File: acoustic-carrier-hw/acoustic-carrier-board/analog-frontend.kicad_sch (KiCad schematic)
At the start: 97 parts, among them J1001 BWU.FL-IPEX1, J1002 BWU.FL-IPEX1, J1003 BWU.FL-IPEX1, J1004 BWU.FL-IPEX1, J1005 BWU.FL-IPEX1, J1006 BWU.FL-IPEX1, J1007 8P8C_Shielded, J1008 BWU.FL-IPEX1, J1009 BWU.FL-IPEX1, J1010 BWU.FL-IPEX1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

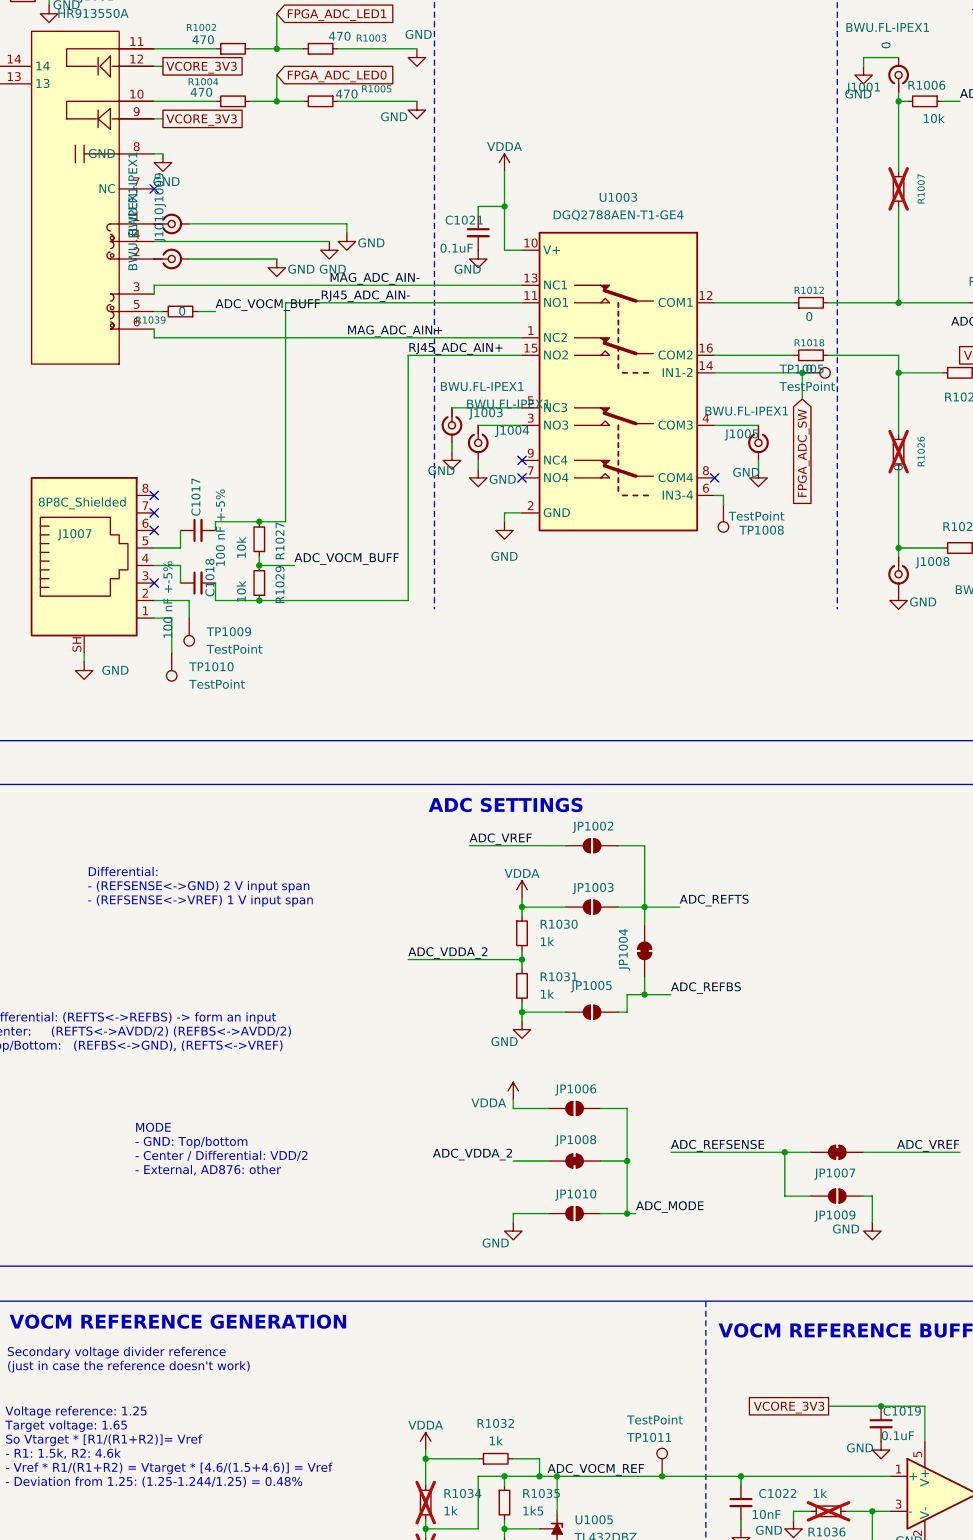
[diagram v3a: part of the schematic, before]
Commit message: [carrier] Layout more or less complete (next) think about adding 6x2 connectors, and add extra pin signals to the connector for testing
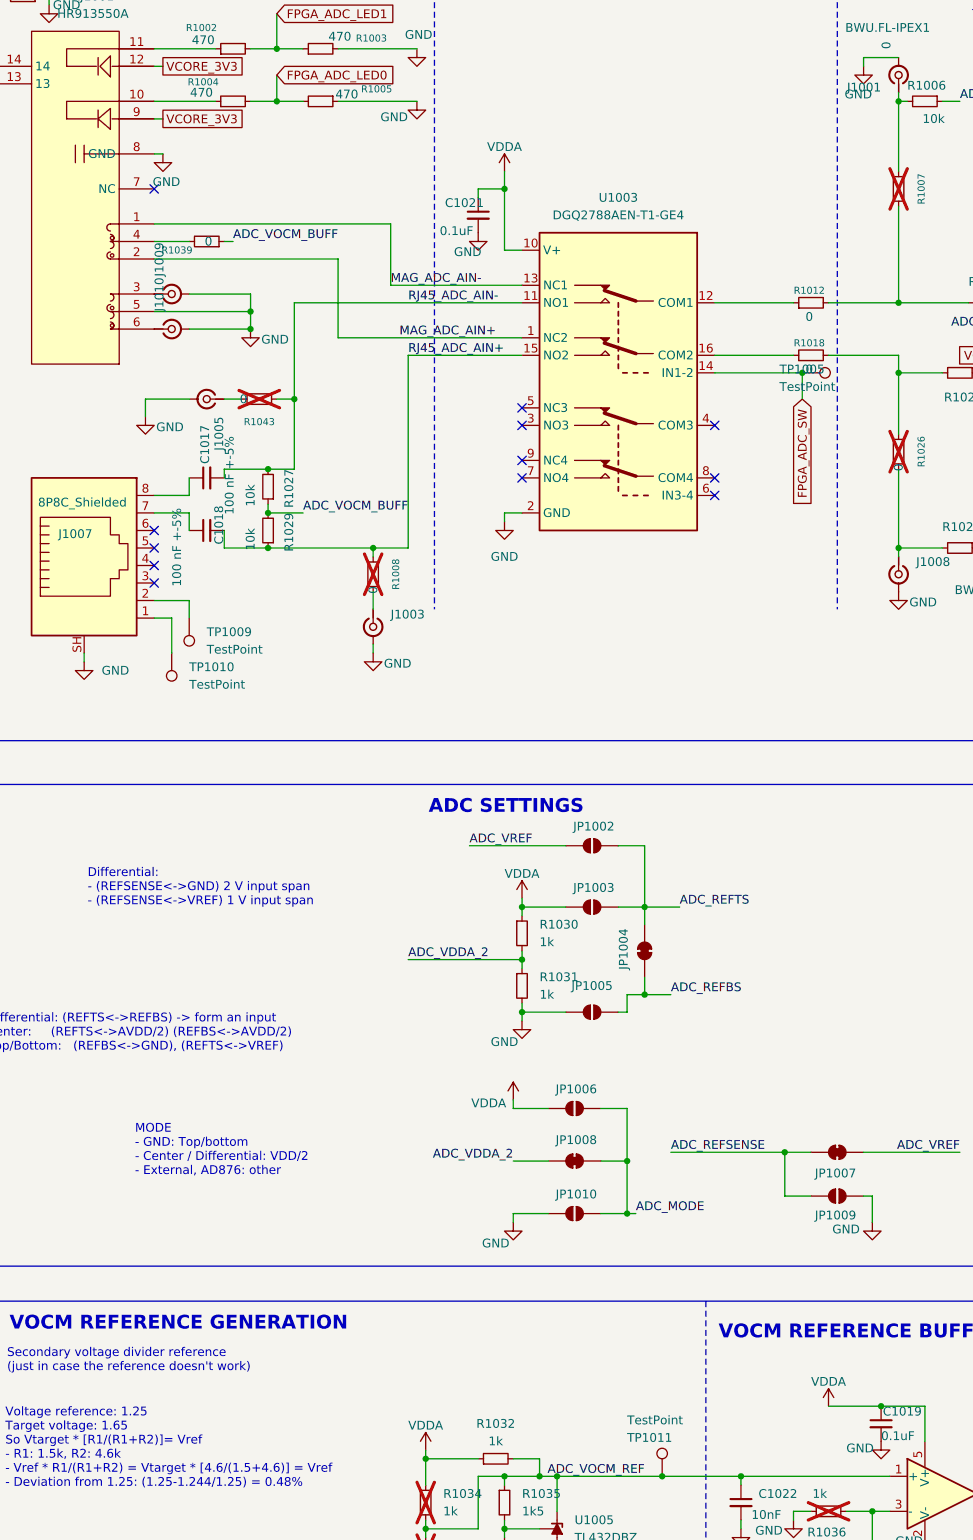
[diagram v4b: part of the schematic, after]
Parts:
- removed J1004: BWU.FL-IPEX1, iw-connector:BWU.FL-IPEX1, symbol Connector:Conn_Coaxial_Small
- removed TP1008: TestPoint, TestPoint:TestPoint_Pad_1.0x1.0mm, symbol Connector:TestPoint
- added R1008, R1043: 0, Resistor_SMD:R_0603_1608Metric, symbol Device:R_Small
- TP1005: footprint TestPoint:TestPoint_Loop_D1.80mm_Drill1.0mm_Beaded -> TestPoint:TestPoint_THTPad_1.5x1.5mm_Drill0.7mm
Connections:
- net GND: now also RJ1001.5; no longer RJ1001.4
- net MAG_ADC_AIN+: now also RJ1001.2; no longer RJ1001.6
- net MAG_ADC_AIN-: now also RJ1001.1; no longer RJ1001.3
- net RJ45_ADC_AIN+: now also R1008.1
- net RJ45_ADC_AIN-: now also R1043.1
- net VCORE_3V3: no longer C1019.1, U1004.5 (V+)
- net VDDA: now also C1019.1, U1004.5 (V+)
- net at J1009.1 (In): now also RJ1001.3; no longer RJ1001.1
- net at J1010.1 (In): now also RJ1001.6; no longer RJ1001.2
- net at R1039.2: now also RJ1001.4; no longer RJ1001.5
- net at U1003.4 (COM3): no longer J1005.1 (In)
- net at C1017.1: now also J1007.8; no longer J1007.5
- net at J1003.1 (In): now also R1008.2; no longer U1003.5 (NC3)
- net at J1007.4: no longer C1018.1
- net at J1007.7: now also C1018.1
- new net: J1005.1 (In), R1043.2
- no-connect marks 8 -> 12
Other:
- moved on the sheet: C1017, C1018, C1021, J1009, J1010, R1027, R1029, R1039
